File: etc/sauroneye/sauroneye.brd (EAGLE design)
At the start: 67 x 60.9 mm, 7 parts

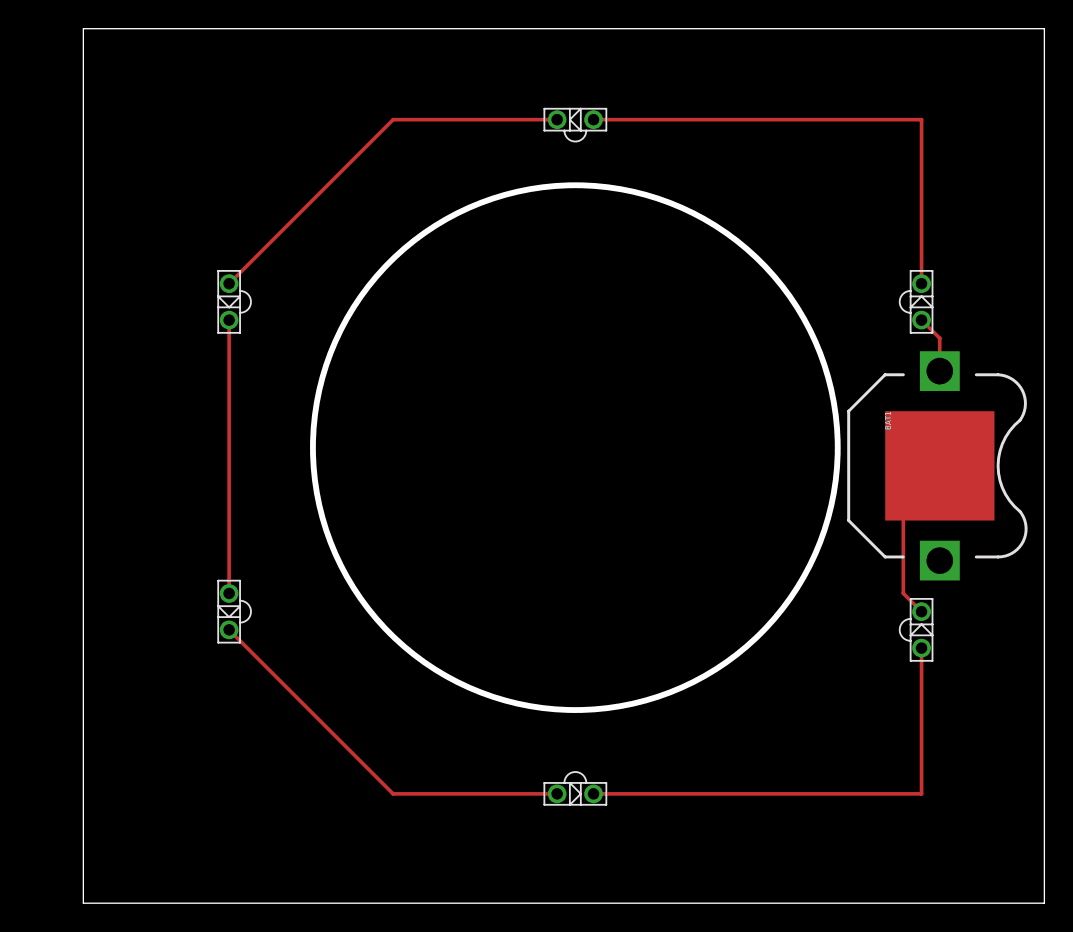
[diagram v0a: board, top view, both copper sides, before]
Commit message: update to board
  * board now obeys physics and laws of electricity
  * board has USB connector
  * removing whatever those spurious eagle files are and ignoring them
    in the future
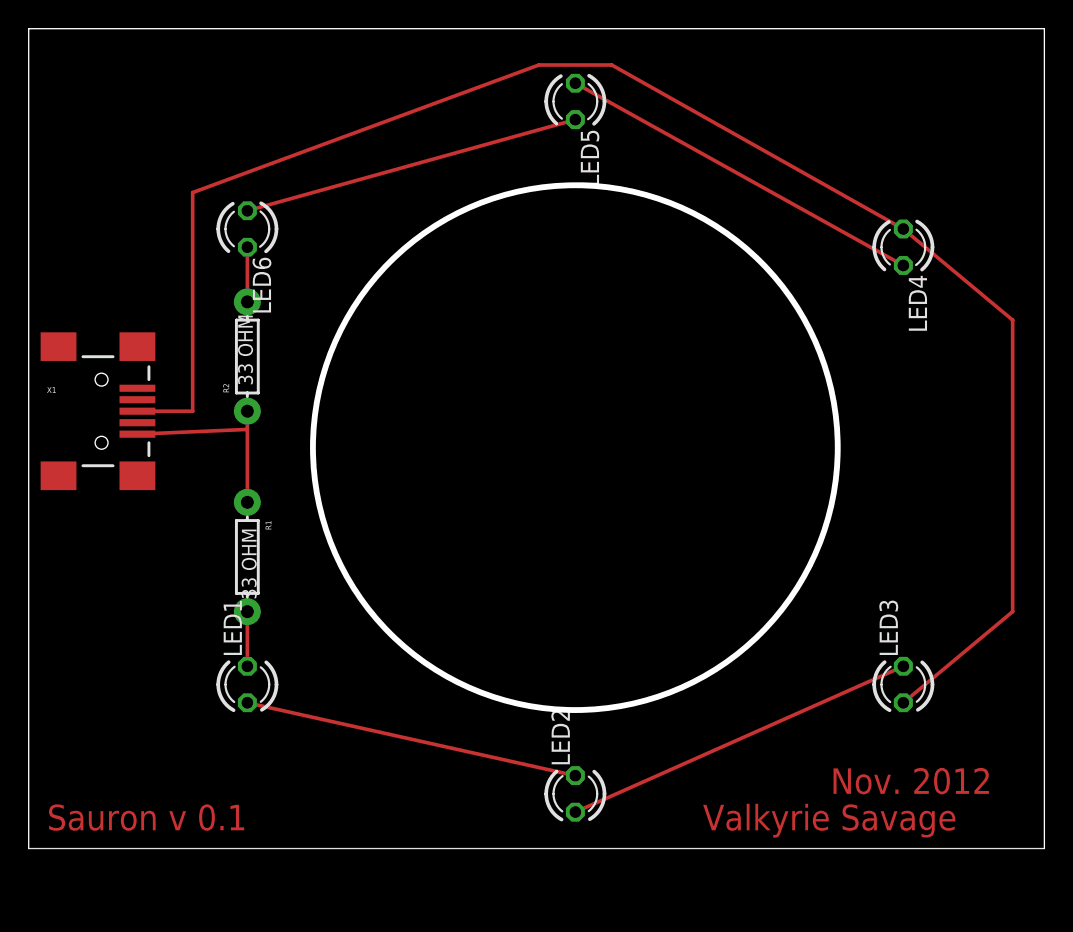
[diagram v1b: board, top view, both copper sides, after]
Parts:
- removed BAT1: (no value), SparkFun-Electromechanical:BATTCON_12MM_PTH
- removed D10, D11, D12, D7, D8, D9: (no value), SparkFun-LED:LTE-302
- added LED1, LED2, LED3, LED4, LED5, LED6: TLLG4400, led:LED3MM
- added R1, R2: 33 OHM, SparkFun:AXIAL-0.3
- added X1: USBSMD, SparkFun:USB-MINIB
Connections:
- removed net N$10: D11.C, D12.A
- removed net N$7: D8.C, D9.A
- removed net N$8: D10.A, D9.C
- removed net N$9: D10.C, D11.A
- new net N$1: LED6.K, R2.P$2
- new net N$2: LED1.K, R1.P$2
- new net N$3: LED5.K, LED6.A
- new net N$4: LED4.K, LED5.A
- new net N$5: LED1.A, LED2.K
- net GND: now also R1.P$1, R2.P$1, X1.GND; no longer BAT1.GND, D12.C
- net N$6: now also LED2.A, LED3.K; no longer D7.C, D8.A
- net VCC: now also LED3.A, LED4.A, X1.D+; no longer BAT1.VCC@1, D7.A
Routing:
- net VCC: track 4.08 -> 113.4 mm
- net N$10: track 33.0 -> 0.00 mm
- net N$7: track 27.6 -> 0.00 mm
- net N$9: track 27.6 -> 0.00 mm
- net N$4: track 0.00 -> 26.2 mm
- net N$3: track 0.00 -> 23.7 mm
- net N$5: track 0.00 -> 23.4 mm
- net N$8: track 19.0 -> 0.00 mm
- net N$6: track 34.3 -> 25.0 mm
- net N$2: track 0.00 -> 3.81 mm
- net N$1: track 0.00 -> 3.81 mm
- net GND: track 11.7 -> 14.0 mm
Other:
- board size 67 x 60.9 mm -> 70.8 x 57.1 mm
- board text added: "Nov. 2012"
- board text added: "Sauron v 0.1"
- board text added: "Valkyrie Savage"
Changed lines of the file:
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@@
 <?xml version="1.0" encoding="utf-8"?>
 <!DOCTYPE eagle SYSTEM "eagle.dtd">
-<eagle version="6.3">
+<eagle version="6.2">
 <drawing>
 <settings>
@@
 <board>
 <plain>
-<wire x1="16.51" y1="11.43" x2="83.49" y2="11.43" width="0" layer="20"/>
-<wire x1="83.49" y1="11.43" x2="83.49" y2="72.38" width="0" layer="20"/>
-<wire x1="83.49" y1="72.38" x2="16.51" y2="72.38" width="0" layer="20"/>
-<wire x1="16.51" y1="72.38" x2="16.51" y2="11.43" width="0" layer="20"/>
+<wire x1="12.7" y1="15.24" x2="83.49" y2="15.24" width="0" layer="25"/>
+<wire x1="83.49" y1="15.24" x2="83.49" y2="72.38" width="0" layer="20"/>
+<wire x1="83.49" y1="72.38" x2="12.7" y2="72.38" width="0" layer="20"/>
+<wire x1="12.7" y1="72.38" x2="12.7" y2="15.24" width="0" layer="20"/>
 <circle x="50.8" y="43.18" radius="18.288" width="0.4064" layer="20"/>
+<text x="13.97" y="16.51" size="1.778" layer="1" ratio="15">Sauron v 0.1</text>
+<text x="59.69" y="16.51" size="1.778" layer="1" ratio="15">Valkyrie Savage</text>
+<text x="68.58" y="19.05" size="1.778" layer="1" ratio="15">Nov. 2012</text>
 </plain>
 <attributes>
@@
 </class>
 </classes>
-<designrules name="default">
+<designrules>
 <description language="de">&lt;b&gt;EAGLE Design Rules&lt;/b&gt;
 &lt;p&gt;
@@
 </autorouter>
 <elements>
-<element name="D7" library="SparkFun-LED" package="LTE-302" value="" x="74.93" y="53.34" rot="R270"/>
-<element name="D8" library="SparkFun-LED" package="LTE-302" value="" x="50.8" y="66.04"/>
-<element name="D9" library="SparkFun-LED" package="LTE-302" value="" x="26.67" y="53.34" rot="R90"/>
-<element name="D10" library="SparkFun-LED" package="LTE-302" value="" x="26.67" y="31.75" rot="R90"/>
-<element name="D11" library="SparkFun-LED" package="LTE-302" value="" x="50.8" y="19.05" rot="R180"/>
-<element name="D12" library="SparkFun-LED" package="LTE-302" value="" x="74.93" y="30.48" rot="R270"/>
-<element name="BAT1" library="SparkFun-Electromechanical" package="BATTCON_12MM_PTH" value="" x="76.2" y="41.91" rot="R270"/>
+<element name="X1" library="SparkFun" package="USB-MINIB" value="USBSMD" x="17.78" y="45.72"/>
+<element name="LED1" library="led" package="LED3MM" value="TLLG4400" x="27.94" y="26.67" rot="R90">
+<attribute name="MF" value="VISHAY SEMICONDUCTOR" x="27.94" y="26.67" size="1.778" layer="27" ratio="15" rot="R90" display="off"/>
+<attribute name="OC_FARNELL" value="1612435" x="27.94" y="26.67" size="1.778" layer="27" ratio="15" rot="R90" display="off"/>
+</element>
+<element name="LED2" library="led" package="LED3MM" value="TLLG4400" x="50.8" y="19.05" rot="R90">
+<attribute name="MF" value="VISHAY SEMICONDUCTOR" x="50.8" y="19.05" size="1.778" layer="27" ratio="15" rot="R90" display="off"/>
+<attribute name="OC_FARNELL" value="1612435" x="50.8" y="19.05" size="1.778" layer="27" ratio="15" rot="R90" display="off"/>
+</element>
+<element name="LED3" library="led" package="LED3MM" value="TLLG4400" x="73.66" y="26.67" rot="R90">
+<attribute name="MF" value="VISHAY SEMICONDUCTOR" x="73.66" y="26.67" size="1.778" layer="27" ratio="15" rot="R90" display="off"/>
+<attribute name="OC_FARNELL" value="1612435" x="73.66" y="26.67" size="1.778" layer="27" ratio="15" rot="R90" display="off"/>
+</element>
+<element name="LED4" library="led" package="LED3MM" value="TLLG4400" x="73.66" y="57.15" rot="R270">
+<attribute name="MF" value="VISHAY SEMICONDUCTOR" x="73.66" y="57.15" size="1.778" layer="27" ratio="15" rot="R270" display="off"/>
+<attribute name="OC_FARNELL" value="1612435" x="73.66" y="57.15" size="1.778" layer="27" ratio="15" rot="R270" display="off"/>
+</element>
+<element name="LED5" library="led" package="LED3MM" value="TLLG4400" x="50.8" y="67.31" rot="R270">
+<attribute name="MF" value="VISHAY SEMICONDUCTOR" x="50.8" y="67.31" size="1.778" layer="27" ratio="15" rot="R270" display="off"/>
+<attribute name="OC_FARNELL" value="1612435" x="50.8" y="67.31" size="1.778" layer="27" ratio="15" rot="R270" display="off"/>
+</element>
+<element name="LED6" library="led" package="LED3MM" value="TLLG4400" x="27.94" y="58.42" rot="R270">
+<attribute name="MF" value="VISHAY SEMICONDUCTOR" x="27.94" y="58.42" size="1.778" layer="27" ratio="15" rot="R270" display="off"/>
+<attribute name="OC_FARNELL" value="1612435" x="27.94" y="58.42" size="1.778" layer="27" ratio="15" rot="R270" display="off"/>
+</element>
+<element name="R1" library="SparkFun" package="AXIAL-0.3" value="33 OHM" x="27.94" y="35.56" rot="R270"/>
+<element name="R2" library="SparkFun" package="AXIAL-0.3" value="33 OHM" x="27.94" y="49.53" rot="R90"/>
 </elements>
 <signals>
+<signal name="VCC">
+<contactref element="X1" pad="D+"/>
+<contactref element="LED3" pad="A"/>
+<contactref element="LED4" pad="A"/>
+<wire x1="73.66" y1="25.4" x2="81.28" y2="31.75" width="0.254" layer="1"/>
+<wire x1="81.28" y1="31.75" x2="81.28" y2="52.07" width="0.254" layer="1"/>
+<wire x1="73.66" y1="58.42" x2="53.34" y2="69.85" width="0.254" layer="1"/>
+<wire x1="53.34" y1="69.85" x2="48.26" y2="69.85" width="0.254" layer="1"/>
+<wire x1="48.26" y1="69.85" x2="24.13" y2="60.96" width="0.254" layer="1"/>
+<wire x1="24.13" y1="60.96" x2="24.13" y2="45.72" width="0.254" layer="1"/>
+<wire x1="24.13" y1="45.72" x2="20.28" y2="45.72" width="0.254" layer="1"/>
+<wire x1="81.28" y1="52.07" x2="73.66" y2="58.42" width="0.254" layer="1"/>
+</signal>
+<signal name="GND">
+<contactref element="X1" pad="GND"/>
+<contactref element="R1" pad="P$1"/>
+<contactref element="R2" pad="P$1"/>
+<wire x1="27.94" y1="45.72" x2="27.94" y2="44.45" width="0.254" layer="1"/>
+<wire x1="27.94" y1="44.45" x2="27.94" y2="39.37" width="0.254" layer="1"/>
+<wire x1="20.28" y1="44.12" x2="27.94" y2="44.45" width="0.254" layer="1"/>
+</signal>
+<signal name="N$1">
+<contactref element="R2" pad="P$2"/>
+<contactref element="LED6" pad="K"/>
+<wire x1="27.94" y1="57.15" x2="27.94" y2="53.34" width="0.254" layer="1"/>
+</signal>
+<signal name="N$2">
+<contactref element="R1" pad="P$2"/>
+<contactref element="LED1" pad="K"/>
+<wire x1="27.94" y1="31.75" x2="27.94" y2="27.94" width="0.254" layer="1"/>
+</signal>
+<signal name="N$3">
+<contactref element="LED6" pad="A"/>
+<contactref element="LED5" pad="K"/>
+<wire x1="50.8" y1="66.04" x2="27.94" y2="59.69" width="0.254" layer="1"/>
+</signal>
+<signal name="N$4">
+<contactref element="LED5" pad="A"/>
+<contactref element="LED4" pad="K"/>
+<wire x1="73.66" y1="55.88" x2="50.8" y2="68.58" width="0.254" layer="1"/>
+</signal>
+<signal name="N$5">
+<contactref element="LED1" pad="A"/>
+<contactref element="LED2" pad="K"/>
+<wire x1="27.94" y1="25.4" x2="50.8" y2="20.32" width="0.254" layer="1"/>
+</signal>
 <signal name="N$6">
-<contactref element="D7" pad="C"/>
-<contactref element="D8" pad="A"/>
-<wire x1="74.93" y1="66.04" x2="52.07" y2="66.04" width="0.254" layer="1"/>
-<wire x1="74.93" y1="54.61" x2="74.93" y2="66.04" width="0.254" layer="1"/>
-</signal>
-<signal name="N$7">
-<contactref element="D8" pad="C"/>
-<contactref element="D9" pad="A"/>
-<wire x1="38.1" y1="66.04" x2="26.67" y2="54.61" width="0.254" layer="1"/>
-<wire x1="49.53" y1="66.04" x2="38.1" y2="66.04" width="0.254" layer="1"/>
-</signal>
-<signal name="N$8">
-<contactref element="D9" pad="C"/>
-<contactref element="D10" pad="A"/>
-<wire x1="26.67" y1="52.07" x2="26.67" y2="33.02" width="0.254" layer="1"/>
-</signal>
-<signal name="N$9">
-<contactref element="D10" pad="C"/>
-<contactref element="D11" pad="A"/>
-<wire x1="38.1" y1="19.05" x2="26.67" y2="30.48" width="0.254" layer="1"/>
-<wire x1="49.53" y1="19.05" x2="38.1" y2="19.05" width="0.254" layer="1"/>
-</signal>
-<signal name="N$10">
-<contactref element="D11" pad="C"/>
-<contactref element="D12" pad="A"/>
-<wire x1="74.93" y1="19.05" x2="52.07" y2="19.05" width="0.254" layer="1"/>
-<wire x1="74.93" y1="29.21" x2="74.93" y2="19.05" width="0.254" layer="1"/>
-</signal>
-<signal name="VCC">
-<contactref element="D7" pad="A"/>
-<contactref element="BAT1" pad="VCC@1"/>
-<wire x1="76.2" y1="50.8" x2="74.93" y2="52.07" width="0.254" layer="1"/>
-<wire x1="76.2" y1="48.514" x2="76.2" y2="50.8" width="0.254" layer="1"/>
-</signal>
-<signal name="GND">
-<contactref element="D12" pad="C"/>
-<contactref element="BAT1" pad="GND"/>
-<wire x1="73.66" y1="33.02" x2="74.93" y2="31.75" width="0.254" layer="1"/>
-<wire x1="73.66" y1="39.37" x2="73.66" y2="33.02" width="0.254" layer="1"/>
-<wire x1="76.2" y1="41.91" x2="73.66" y2="39.37" width="0.254" layer="1"/>
+<contactref element="LED2" pad="A"/>
+<contactref element="LED3" pad="K"/>
+<wire x1="50.8" y1="17.78" x2="73.66" y2="27.94" width="0.254" layer="1"/>
 </signal>
 </signals>
